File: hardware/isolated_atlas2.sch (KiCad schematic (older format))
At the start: 14 parts, among them J401 CONN_01X02, U401 adm3260, U402 ATLAS_SENSOR

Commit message: Fix SSOP-20 width on the isolator.
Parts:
- U401: footprint SMD_Packages:SSOP-20 -> conservify:SSOP20-53
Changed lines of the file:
@@
 F 0 "U401" H 4400 2750 60  0000 C CNN
 F 1 "adm3260" H 4400 2900 60  0000 C CNN
-F 2 "SMD_Packages:SSOP-20" H 4400 2900 60  0001 C CNN
+F 2 "conservify:SSOP20-53" H 4400 2900 60  0001 C CNN
 F 3 "" H 4400 2900 60  0001 C CNN
 F 4 "584-ADM3260ARSZ" H 0   0   50  0001 C CNN "spn1"

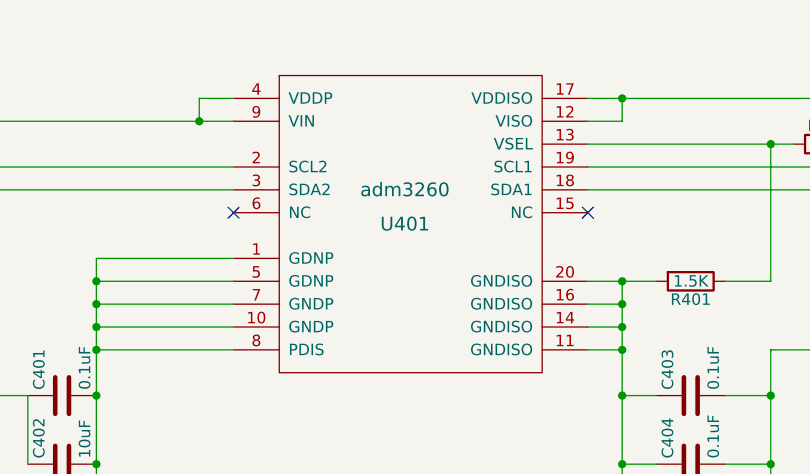
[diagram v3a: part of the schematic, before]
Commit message: Fixing some component names.
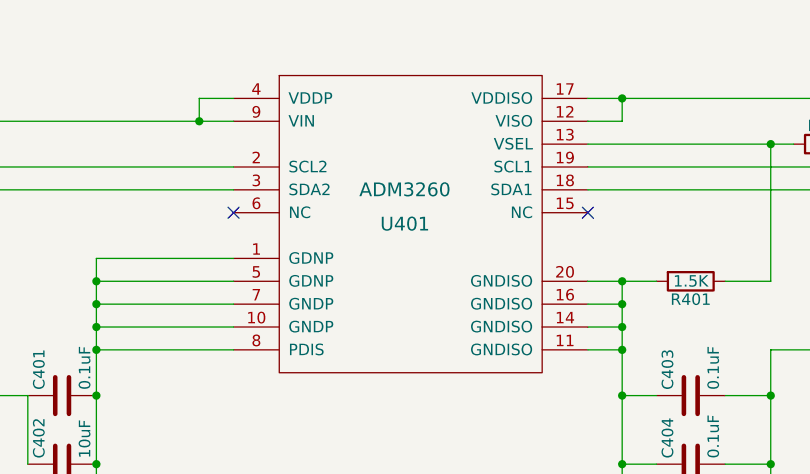
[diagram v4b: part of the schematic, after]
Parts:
- C401, C402, C403, C404, C405, C406, J401, R401, R402, R403, R404, R405, U402: price (none) -> 0
- U401: value adm3260 -> ADM3260; price (none) -> 0

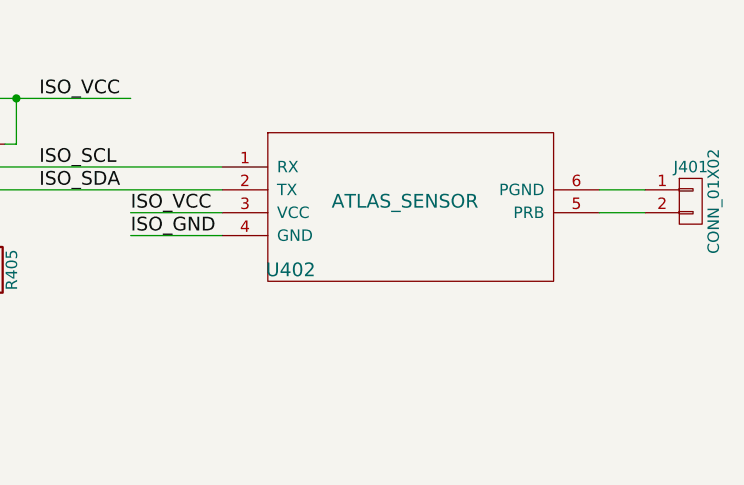
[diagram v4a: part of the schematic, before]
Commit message: Individual atlas sensor values for costing.
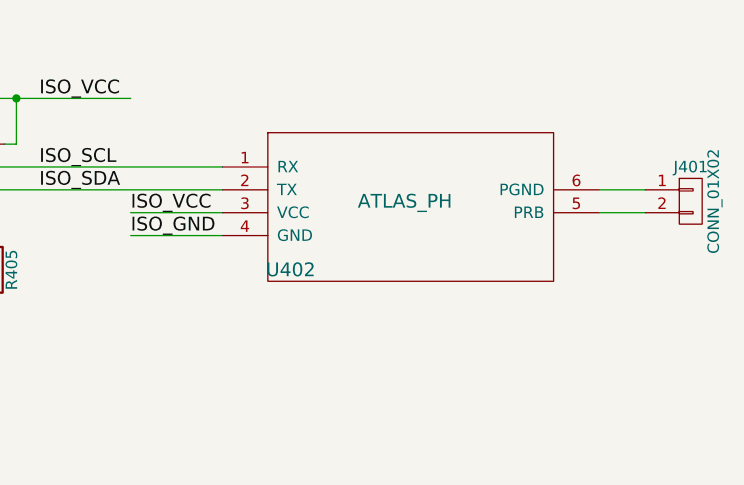
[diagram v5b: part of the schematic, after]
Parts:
- U402: value ATLAS_SENSOR -> ATLAS_PH

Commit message: Normalizing some passive footprints.
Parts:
- C401, C403, C404: footprint Resistors_SMD:R_0603_HandSoldering -> Capacitors_SMD:C_0603_HandSoldering
- C402, C405, C406: footprint Resistors_SMD:R_0603_HandSoldering -> Capacitors_SMD:C_0603_HandSoldering; spn1 810-C1608X7S0J106M -> 81-GRM188R60J106ME47

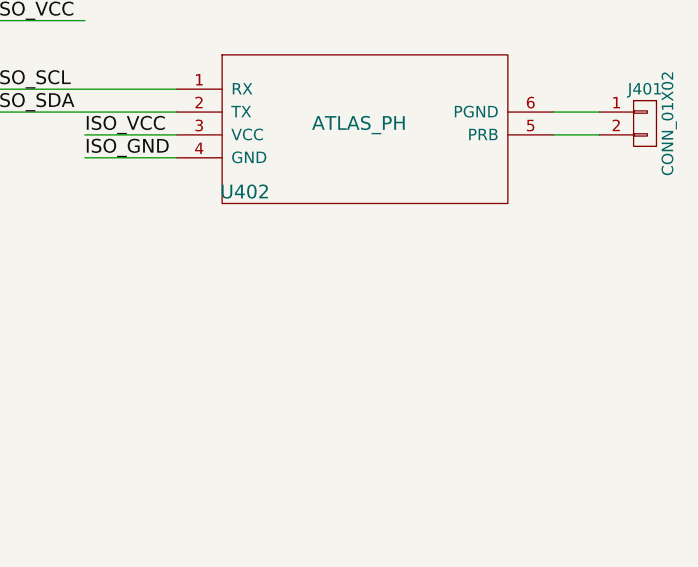
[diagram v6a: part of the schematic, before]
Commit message: Adding placeholders for probes for the BOM.
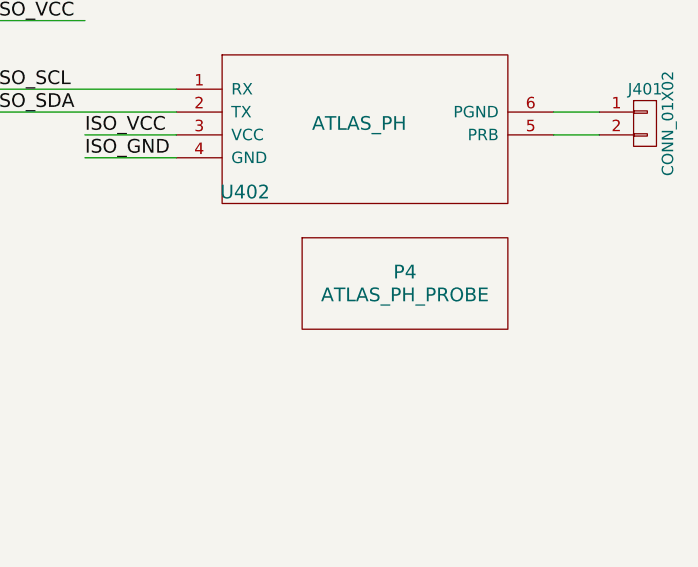
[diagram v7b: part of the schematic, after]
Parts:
- added P4: ATLAS_PH_PROBE, Oddities:Dummy_Empty, symbol WATER_PROBE

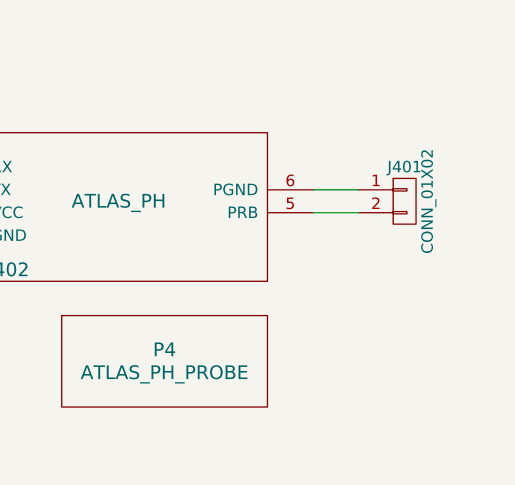
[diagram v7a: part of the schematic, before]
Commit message: Add footprint for OEM Atlas Circuit.
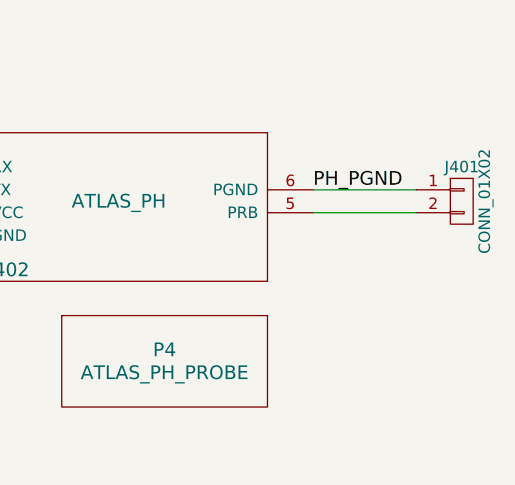
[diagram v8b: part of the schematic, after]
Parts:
- U402: footprint conservify:atlas_sensor_board -> conservify:ATLAS_SENSOR_BOARD_COMBO
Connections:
- net labels added: PH_PGND
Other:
- moved on the sheet: J401
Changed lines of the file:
@@
 F 0 "U402" H 8100 2550 60  0000 C CNN
 F 1 "ATLAS_PH" H 8600 2850 60  0000 C CNN
-F 2 "conservify:atlas_sensor_board" H 8550 2900 60  0001 C CNN
+F 2 "conservify:ATLAS_SENSOR_BOARD_COMBO" H 8550 2900 60  0001 C CNN
 F 3 "" H 8550 2900 60  0001 C CNN
 F 4 "0" H 8100 2650 50  0001 C CNN "price"
@@
 L CONN_01X02 J401
 U 1 1 59A1BC7D
-P 9850 2950
-F 0 "J401" H 9850 3100 50  0000 C CNN
-F 1 "CONN_01X02" V 9950 2950 50  0000 C CNN
-F 2 "conservify:BNC" H 9850 2950 50  0001 C CNN
-F 3 "" H 9850 2950 50  0001 C CNN
-F 4 "0" H 9850 3200 50  0001 C CNN "price"
-F 5 "523-31-5431" H 0   0   50  0001 C CNN "spn1"
-	1    9850 2950
+P 10100 2950
+F 0 "J401" H 10100 3100 50  0000 C CNN
+F 1 "CONN_01X02" V 10200 2950 50  0000 C CNN
+F 2 "conservify:BNC" H 10100 2950 50  0001 C CNN
+F 3 "" H 10100 2950 50  0001 C CNN
+F 4 "0" H 10100 3200 50  0001 C CNN "price"
+F 5 "523-31-5431" H 250 0   50  0001 C CNN "spn1"
+	1    10100 2950
 	1    0    0    -1
 $EndComp
@@
 	7400 3000 7800 3000
 Wire Wire Line
-	9450 2900 9650 2900
+	9450 2900 9900 2900
 Wire Wire Line
-	9650 3000 9450 3000
+	9450 3000 9900 3000
 Connection ~ 5350 3500
 Connection ~ 5350 3400
@@
 	1    0    0    -1
 $EndComp
+Text Label 9450 2900 0    60   ~ 0
+PH_PGND
 $EndSCHEMATC
